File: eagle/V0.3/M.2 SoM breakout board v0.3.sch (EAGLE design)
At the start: 165 parts, among them J1 3-PIN SMD, J10 CON_122_SMD_HEADER, J11 WAFER-HY2.0-4PWB, J12 TP_OPEN, J13 SIM-NANO-4FF, J15 CON_122_SMD_HEADER, J16 SIP-2, J18 PARTICLE-STUDIOS_M_SERIES_M.2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, J19 TP_OPEN, J2 DCJ0202, J20 TP_OPEN, J21 SIP-2, J22 SIP-2, J3 SPARK_CON_30X2_SMD, J5 SCREW-HOLE-3.7, J6 PARTICLE-SZ_PARTICLE-POWER-MO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, J7 SCREW-HOLE-3.7, J8 TP_OPEN, Q3 HSS2333, Q4 HSS2333, Q5 HSS2333, T1 TP_SHORT, U1 XC8107, U2 AT24CS64-SSHM-B, U7 NC, X1 BU-SMA-G, X2 BU-SMA-G, X3 BU-SMA-G

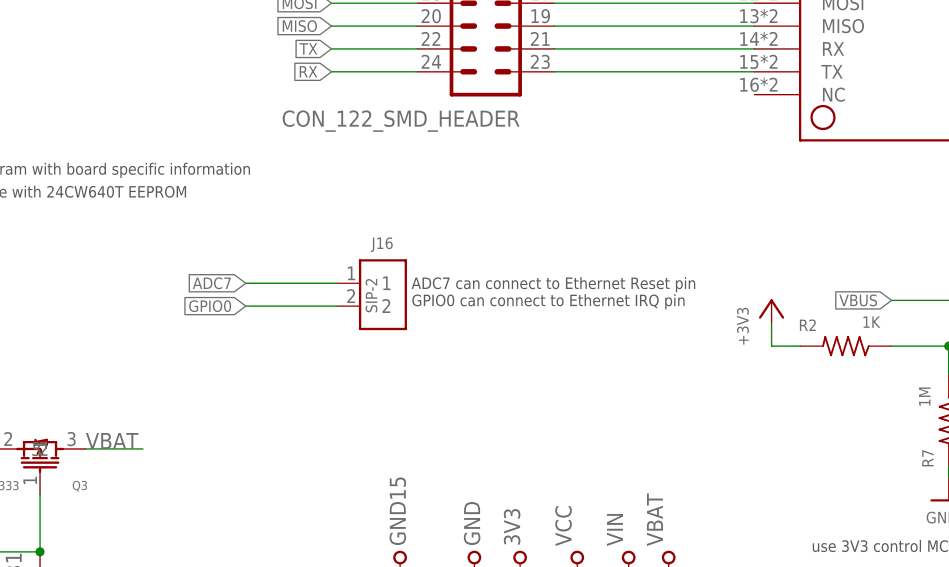
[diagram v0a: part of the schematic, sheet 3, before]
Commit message: update
  delete based test:
  2 pinholes for jumpers ，GPIO0  is used for IRQ ADC7   is used for RESET  that is no needed
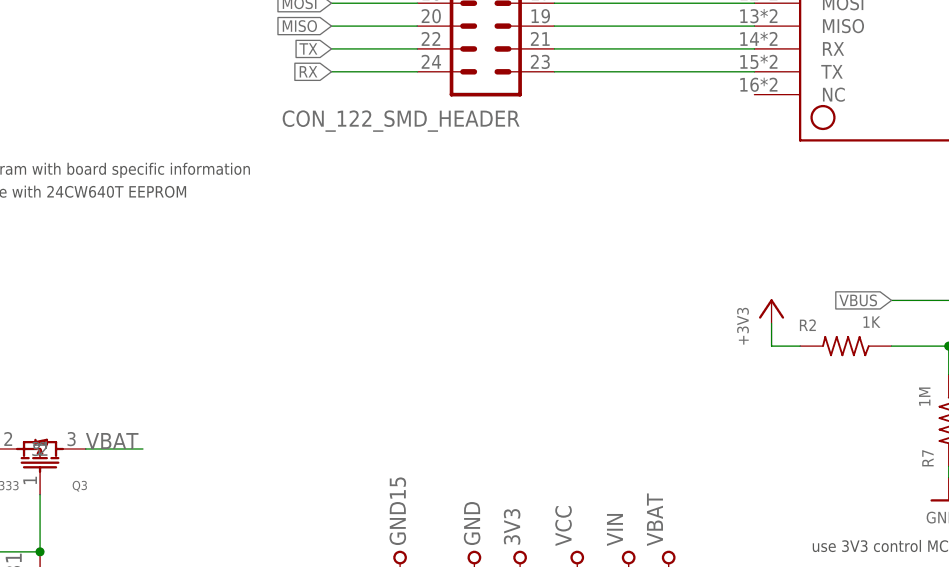
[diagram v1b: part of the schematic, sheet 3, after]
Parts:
- removed J16: SIP-2, particle SZ:SIP-2
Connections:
- net ADC7: no longer J16.1
- net GPIO0: no longer J16.2
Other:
- note removed: "ADC7 can connect to Ethernet Reset pin GPIO0 can connect to Ethernet IRQ pin"
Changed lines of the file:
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@@
 <part name="J1" library="SparkFun-Connectors" library_urn="urn:adsk.eagle:library:513" deviceset="CONN_03" device="JST-SMD" package3d_urn="urn:adsk.eagle:package:38075/1" value="3-PIN SMD"/>
 <part name="JP4" library="particle SZ" library_urn="urn:adsk.eagle:library:21650216" deviceset="TP_SHORT" device="" package3d_urn="urn:adsk.eagle:package:21650878/5"/>
-<part name="J16" library="particle SZ" library_urn="urn:adsk.eagle:library:21650216" deviceset="SIP-2" device="" package3d_urn="urn:adsk.eagle:package:21650858/5"/>
 <part name="JP9" library="particle SZ" library_urn="urn:adsk.eagle:library:21650216" deviceset="TP_SHORT" device="" package3d_urn="urn:adsk.eagle:package:21650878/5" value="TP_SHORT"/>
 </parts>
@@
 </instance>
 <instance part="J18" gate="G$1" x="118.745" y="106.68" smashed="yes">
-<attribute name="NAME" x="98.425" y="53.34" size="1.778" layer="95"/>
-<attribute name="VALUE" x="98.425" y="50.8" size="1.778" layer="96"/>
+<attribute name="NAME" x="99.695" y="53.34" size="1.778" layer="95"/>
+<attribute name="VALUE" x="98.425" y="50.8" size="1.778" layer="96" display="off"/>
 </instance>
 <instance part="J18" gate="G$2" x="53.34" y="102.87" smashed="yes" rot="MR180"/>
@@
 <text x="238.76" y="63.5" size="1.27" layer="97">23 Reserve for reset
 power module</text>
-<text x="125.73" y="104.775" size="1.27" layer="97">ADC7 can connect to Ethernet Reset pin
-GPIO0 can connect to Ethernet IRQ pin</text>
 </plain>
 <instances>
@@
 <attribute name="NAME" x="36.195" y="73.152" size="1.778" layer="95" font="vector" rot="R180"/>
 </instance>
-<instance part="J16" gate="G$1" x="122.555" y="106.045" smashed="yes">
-<attribute name="NAME" x="121.285" y="111.125" size="1.27" layer="95"/>
-<attribute name="VALUE" x="120.65" y="107.95" size="1.27" layer="96" rot="R270"/>
-</instance>
 </instances>
 <busses>
@@
 <pinref part="J10" gate="G$1" pin="19"/>
 </segment>
-<segment>
-<wire x1="117.475" y1="104.775" x2="107.315" y2="104.775" width="0.1524" layer="91"/>
-<label x="107.315" y="104.775" size="1.27" layer="95" rot="R180" xref="yes"/>
-<pinref part="J16" gate="G$1" pin="2"/>
-</segment>
 </net>
 <net name="GPIO1" class="0">
@@
 </segment>
 </net>
-<net name="ADC7" class="0">
-<segment>
-<wire x1="117.475" y1="107.315" x2="107.315" y2="107.315" width="0.1524" layer="91"/>
-<label x="107.315" y="107.315" size="1.27" layer="95" rot="R180" xref="yes"/>
-<pinref part="J16" gate="G$1" pin="1"/>
-</segment>
-</net>

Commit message: update
update SCH&PCB
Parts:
- removed J8: TP_OPEN, particle SZ:TP_OPEN
- removed JP9: TP_SHORT, particle SZ:TP_SHORT
- removed LED2: BLUE, particle SZ:LED
- removed R22: 10K, particle-studios:RES_10K_0603
- removed R32: nc, particle SZ:RES0402S
- added Q1: HSS2333, RedBear:PMOS
- added R17: 1K, Particle:R-US_
- added TP1, TP2, TP5, TP8: TPTPEB, particle SZ:TPTPEB
- R11: value 1K -> 100K
- R18: value nc -> 6.91K; device particle SZ:RES0402S -> particle SZ:RESR0603
- R74: value nc -> 83.2K; device particle SZ:RES0402S -> particle SZ:RESR0603
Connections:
- removed net 5VDC: J6.5DC@3, J6.5DC@4
- removed net N$44: R16.2, T1.2
- removed net N$59: JP9.2, R11.2
- removed net NC: J6.NC@8
- new net 3V3_AUX: J11.2, J3.8, J4.2, J6.3V3@2, MS1.3V3, TP30.PP
- net +3V3: no longer J11.2, J3.8, J4.2, J6.3V3@2, MS1.3V3, TP30.PP
- net GND: now also TP8.1; no longer LED2.K, R22.1
- net GPIO1: now also J6.REGN@7
- net N$13: now also J21.2, TP2.1, TP5.1; no longer R32.1
- net N$14: now also Q1.2, R11.2, T1.2; no longer J8.2, R32.2
- net N$18: now also Q1.3, R16.2; no longer R15.1, S1.3, S1.6
- net N$36: now also Q1.1, R17.2; no longer LED2.A
- net N$57: now also R15.1, R17.1, S1.3, S1.6; no longer J21.2, R22.2
- net PWM3: no longer JP9.1
- net REGN: now also J6.NC@8, TP1.1; no longer J6.REGN@7
- net TS: no longer J8.1
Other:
- note added: "GPIO1 is used for ctroling the power module EN_AUX which make load switch work"
- note removed: "If LiPo TS pin don't have 10K NTC connect to GND, connect this jumper,"
- moved on the sheet: 3V3, D17, D4, F5, GND, GND15, J1, J2, J21, J5, J7, Q3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

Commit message: update
update PCB&SCH
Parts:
- added R22: NC, Particle:R-US_
- added RT1: 6.91K, particle SZ:RESR0603
- J11: device M.2 SoM breakout board v0.2-0228:WAFER-HY2.0-4PWB -> M.2 SoM breakout board v0.3:M.2-SOM-BREAKOUT-BOARD-V0.2-0228_WAFER-HY2.0-4PWB
- R18: value 6.91K -> NC; device particle SZ:RESR0603 -> Particle:R-US_
- renumbered R74 to RT2
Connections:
- removed net N$19 (its old number): LED1.A, R16.1
- new net N$36: LED1.K, Q1.2, R22.2
- new net N$44: J6.5DC@3
- new net N$59: J6.5DC@4
- net GND: now also Q1.3, R17.1, R22.1; no longer LED1.K
- net N$13: now also RT1.1; no longer R18.1
- net N$14: now also R16.2; no longer Q1.2, R11.2
- net N$18: now also LED1.A, R16.1, R18.1; no longer Q1.3, R16.2
- net N$57: no longer R17.1
- net PWM1: now also J10.7; no longer J10.11
- net PWM2: now also J10.11; no longer J10.7
- net REGN: now also RT1.2; no longer R18.2
- net VIN: now also R11.2, R18.2
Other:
- note added: "0.3 version"
- note added: "1.3V3 is divided into one channel as the load conversion switch 3V3_AUX, and GPIO1 is added to control EN_AUX 2. Change the peripheral power supply to load 3V3_AUX 3. Remove LED2 (required by nick) 4.LED1 only lights up when DC_JACK, add NMOS control 5. Modify the TS pin configuration and add reserved plug-in resistor vacancies. 6.J10 exchanges the positions of PWM1 and PWM2 and aligns with pinma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"
- note removed: "10"
- note removed: "11"
- note removed: "4"
- note removed: "5"
- note removed: "6"
- note removed: "7"
- note removed: "8"
- note removed: "9"
- moved on the sheet: J11, LED1, Q1, R11, R16, R17, T1

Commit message: Update
Update SCH&PCB
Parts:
- F5: device adafruit:PTCFUSE-1206 -> adafruit:PTCFUSE-1812
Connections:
- net !RESET: now also J15.2
- net SOM17: no longer J15.2
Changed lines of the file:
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@@
 <layer number="13" name="Route13" color="21" fill="1" visible="no" active="no"/>
 <layer number="14" name="Route14" color="22" fill="1" visible="no" active="no"/>
-<layer number="15" name="Route15" color="23" fill="1" visible="no" active="no"/>
+<layer number="15" name="Route15" color="30" fill="1" visible="no" active="no"/>
 <layer number="16" name="Bottom" color="1" fill="1" visible="no" active="no"/>
 <layer number="17" name="Pads" color="2" fill="1" visible="no" active="no"/>
@@
 <part name="D17" library="particle-studios" library_urn="urn:adsk.eagle:library:10700396" deviceset="DIODE-ZENER" device="" package3d_urn="urn:adsk.eagle:package:18150248/1" value="SMAJ15CA-13-F"/>
 <part name="GND3" library="supply1" deviceset="GND" device=""/>
-<part name="F5" library="adafruit" library_urn="urn:adsk.eagle:library:420" deviceset="PTCFUSE" device="-1206" package3d_urn="urn:adsk.eagle:package:6240569/1" value="16V/0.75A"/>
+<part name="F5" library="adafruit" library_urn="urn:adsk.eagle:library:420" deviceset="PTCFUSE" device="-1812" package3d_urn="urn:adsk.eagle:package:6240348/1" value="16V/0.75A"/>
 <part name="U$5" library="microbuilder" deviceset="GND" device=""/>
 <part name="U$8" library="microbuilder" deviceset="GND" device=""/>
@@
 6.J10 exchanges the positions of
  PWM1 and PWM2 and aligns with pinmap
-7. modify the layout</text>
+7. modify the layout
+8.change the reset PIN of featherWing</text>
 </plain>
 <instances>
@@
 <pinref part="J6" gate="G$1" pin="!RST@23"/>
 </segment>
+<segment>
+<wire x1="126.365" y1="158.75" x2="116.84" y2="158.75" width="0.1524" layer="91"/>
+<label x="116.84" y="158.75" size="1.27" layer="95" rot="R180" xref="yes"/>
+<pinref part="J15" gate="G$1" pin="2"/>
+</segment>
 </net>
 <net name="N$45" class="0">
@@
 </segment>
 </net>
-<net name="SOM17" class="0">
-<segment>
-<wire x1="126.365" y1="158.75" x2="116.84" y2="158.75" width="0.1524" layer="91"/>
-<label x="116.84" y="158.75" size="1.27" layer="95" rot="R180" xref="yes"/>
-<pinref part="J15" gate="G$1" pin="2"/>
-</segment>
-</net>

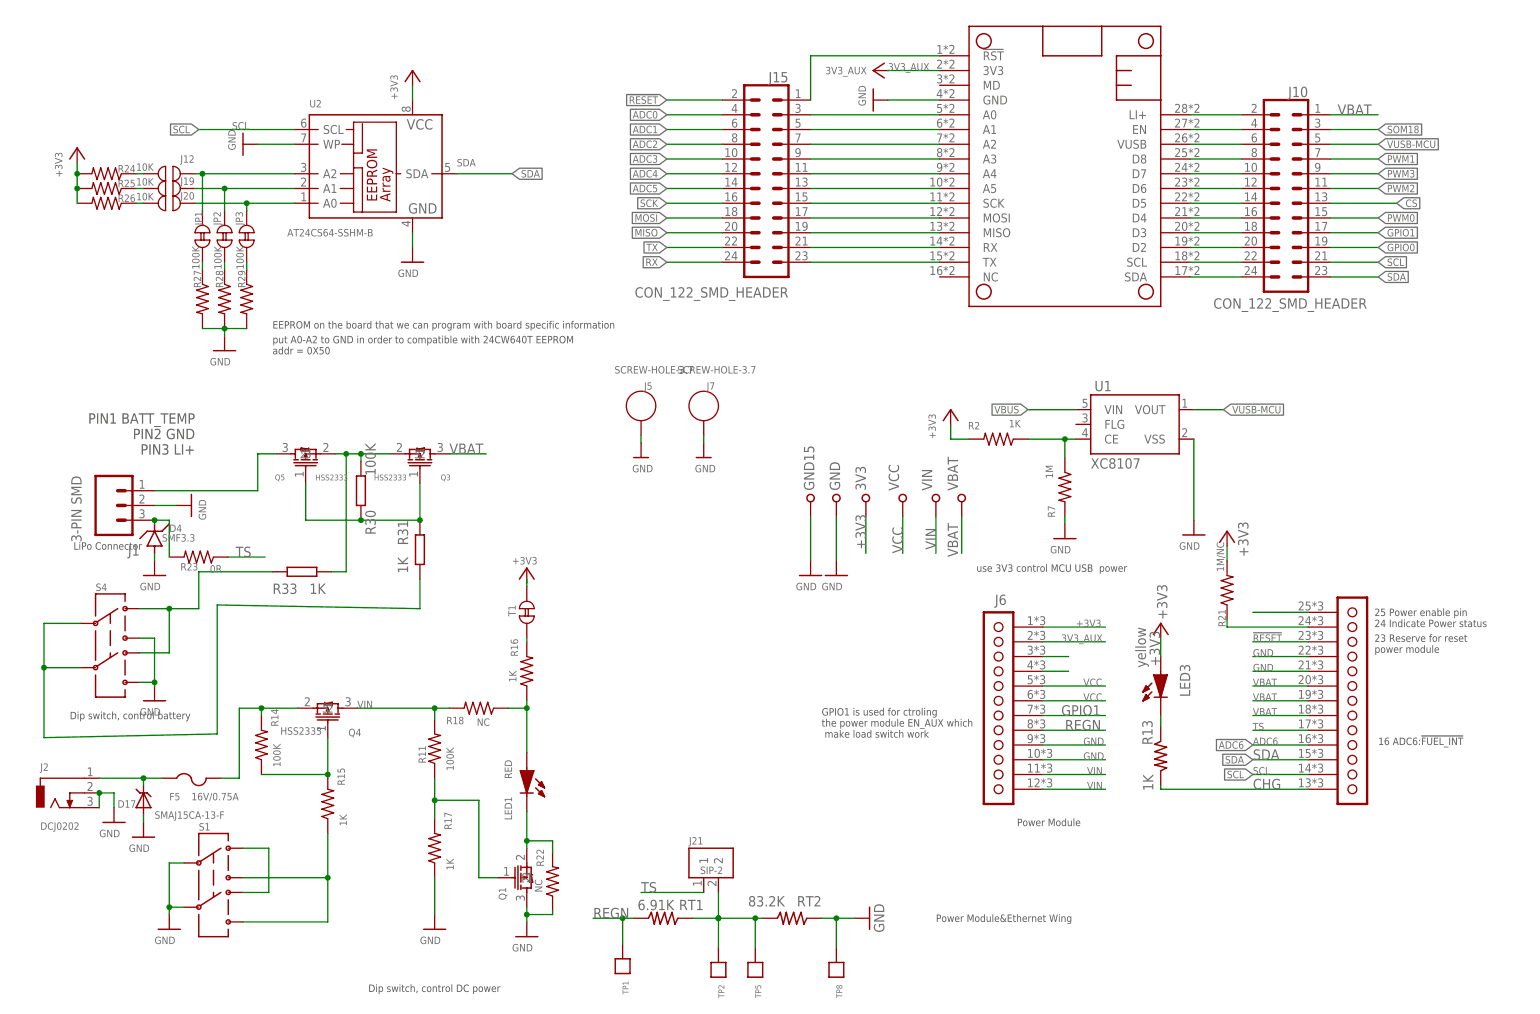
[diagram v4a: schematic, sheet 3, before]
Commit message: updated v0.3 design
1. Change feather jumpers to smd scratch pads
2. Align proto area with m.2
3. Add 3.3V and GND rail along the proto area
4. LiPo battery pinout change - when we changed from vertical to horizontal, the pinout was flipped. so this is now fixed.
5. Flipped the TX/RX to match the feather pin out
6. Removed EN pin connection to feather
7. Align RGB LED and buttons
8. Align the mounting holes to the corners of the PCB
9. Updated silkscreen and pinout labels on top and bottom
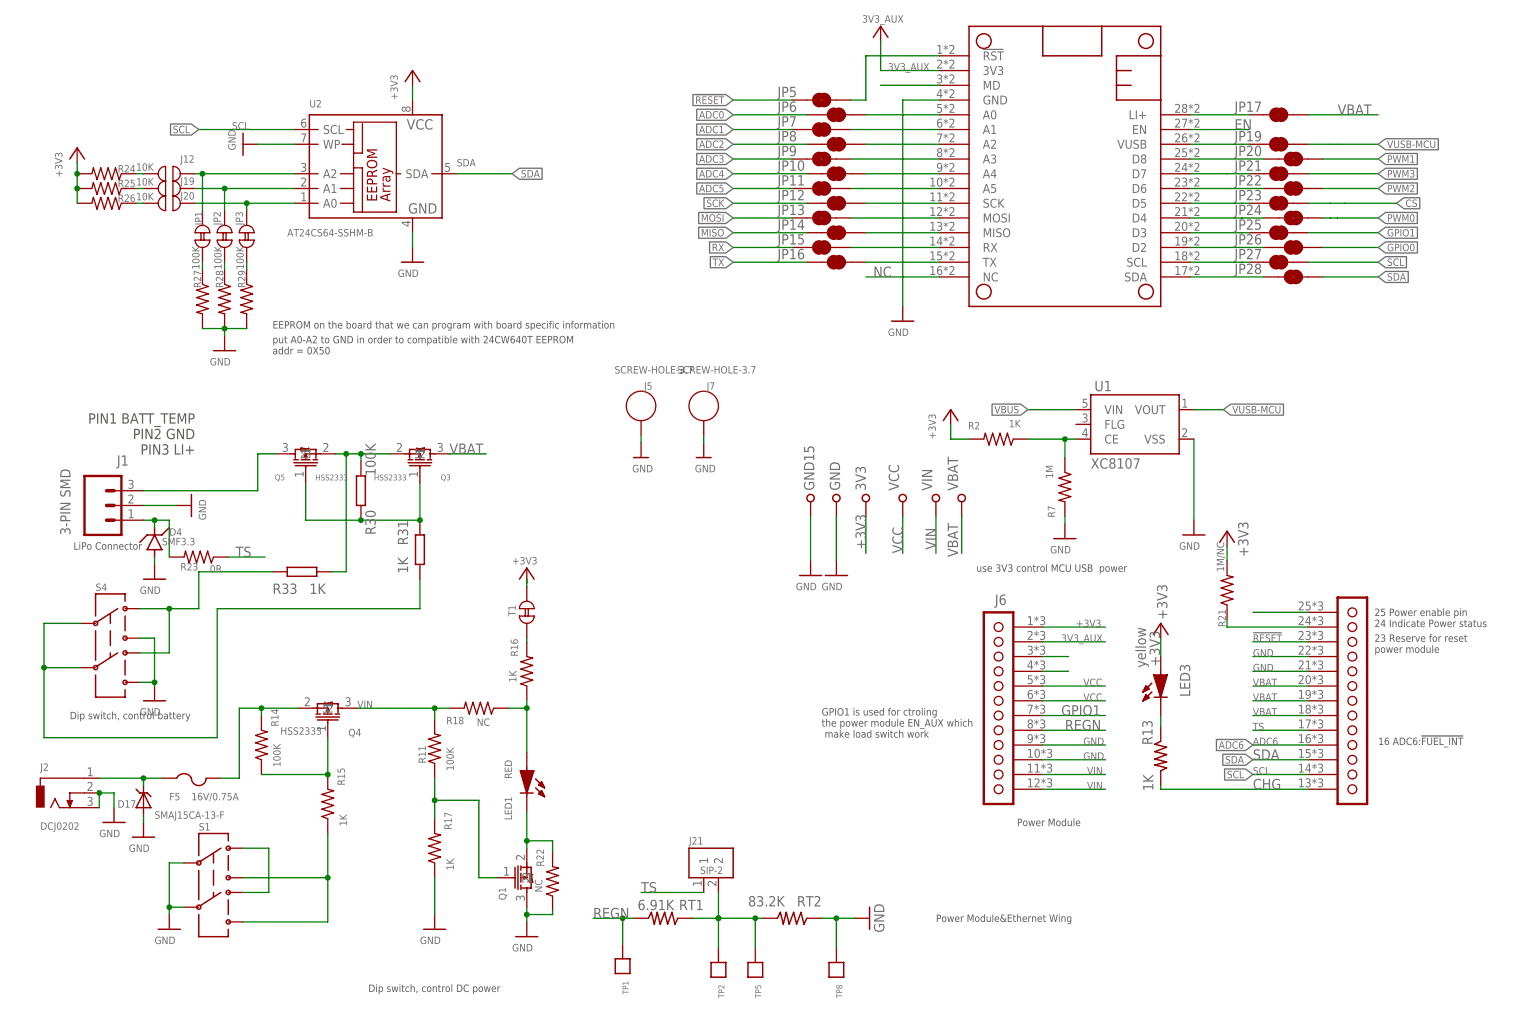
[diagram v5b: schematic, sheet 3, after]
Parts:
- removed J10, J15: CON_122_SMD_HEADER, Spark:CON_122_SMD_HEADER
- added JP10, JP11, JP12, JP13, JP14, JP15, JP16, JP17, JP19, JP20, JP21, JP22, JP23, JP24, JP25, JP26, JP27, JP28, JP5, JP6, JP7, JP8, JP9: JUMPER-SMT_2_NC_TRACE_NO-SILK, SparkFun-Jumpers:JUMPER-SMT_2_NC_TRACE_NO-SILK
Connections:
- removed net N$43: J10.4, MS1.EN
- new net EN: MS1.EN
- new net N$223: D4.C, J1.1, R23.2
- new net NC: MS1.NC
- net !RESET: now also JP5.1; no longer J15.2
- net ADC0: now also JP6.1; no longer J15.4
- net ADC1: now also JP7.1; no longer J15.6
- net ADC2: now also JP8.1; no longer J15.8
- net ADC3: now also JP9.1; no longer J15.10
- net ADC4: now also JP10.1; no longer J15.12
- net ADC5: now also JP11.1; no longer J15.14
- net CS: now also JP23.2; no longer J10.13
- net GPIO0: now also JP26.2; no longer J10.19
- net GPIO1: now also JP25.2; no longer J10.17
- net LI+: now also JP17.1; no longer J10.2
- net MISO: now also JP14.1; no longer J15.20
- net MOSI: now also JP13.1; no longer J15.18
- net N$16: now also JP21.1; no longer J10.10
- net N$21: now also JP6.2; no longer J15.3
- net N$23: now also JP7.2; no longer J15.5
- net N$24: now also JP8.2; no longer J15.7
- net N$25: now also JP9.2; no longer J15.9
- net N$26: now also JP10.2; no longer J15.11
- net N$27: now also JP11.2; no longer J15.13
- net N$28: now also JP12.2; no longer J15.15
- net N$29: now also JP13.2; no longer J15.17
- net N$30: now also JP14.2; no longer J15.19
- net N$31: now also JP15.2; no longer J15.21
- net N$32: now also JP16.2; no longer J15.23
- net N$34: now also JP28.1; no longer J10.24
- net N$35: now also JP27.1; no longer J10.22
- net N$37: now also JP26.1; no longer J10.20
- net N$38: now also JP25.1; no longer J10.18
- net N$39: now also JP24.1; no longer J10.16
- net N$40: now also JP23.1; no longer J10.14
- net N$41: now also JP22.1; no longer J10.12
- net N$42: now also JP20.1; no longer J10.8
- net N$46: now also JP5.2; no longer J15.1
- net N$58: now also J1.3; no longer J1.1
- net N$7: now also MS1.MD; no longer D4.C, J1.3, R23.2
- net PWM0: now also JP24.2; no longer J10.15
- net PWM1: now also JP20.2; no longer J10.7
- net PWM2: now also JP22.2; no longer J10.11
- net PWM3: now also JP21.2; no longer J10.9
- net RX: now also JP15.1; no longer J15.24
- net SCK: now also JP12.1; no longer J15.16
- net SCL: now also JP27.2; no longer J10.21
- net SDA: now also JP28.2; no longer J10.23
- net SOM18: no longer J10.3
- net TX: now also JP16.1; no longer J15.22
- net V-USB: now also JP19.1; no longer J10.6
- net VBAT: now also JP17.2; no longer J10.1
- net VUSB-MCU: now also JP19.2; no longer J10.5
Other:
- moved on the sheet: D4, J1

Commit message: update
update
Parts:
- removed TP10, TP11, TP12, TP13, TP14, TP15, TP16, TP17, TP18, TP19, TP20, TP21, TP22, TP23, TP24, TP25, TP26, TP27, TP28, TP29, TP3, TP30, TP31, TP32, TP33, TP34, TP35, TP36, TP37, TP38, TP39, TP4, TP40, TP41, TP42, TP43, TP44, TP45, TP46, TP47, TP48, TP49, TP50, TP51, TP52, TP53, TP54, TP57, TP6, TP7, TP9: TPSB1,27, testpad:TPSB1,27
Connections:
- net !MODE: no longer TP35.PP
- net !RESET: no longer TP36.PP
- net 3V3_AUX: no longer TP30.PP
- net ADC0: no longer TP6.PP
- net ADC1: no longer TP7.PP
- net ADC2: no longer TP9.PP
- net ADC3: no longer TP10.PP
- net ADC4: no longer TP12.PP
- net ADC5: no longer TP13.PP
- net ADC7: no longer TP15.PP
- net CS: no longer TP41.PP
- net CTS: no longer TP39.PP
- net GND: no longer TP11.PP, TP16.PP, TP29.PP, TP45.PP
- net GPIO0: no longer TP48.PP
- net GPIO1: no longer TP49.PP
- net LED_BLUE: no longer TP24.PP
- net LED_GREEN: no longer TP23.PP
- net LED_RED: no longer TP22.PP
- net MISO: no longer TP42.PP
- net MOSI: no longer TP43.PP
- net N$15: no longer TP14.PP
- net NFC1: no longer TP3.PP
- net NFC2: no longer TP4.PP
- net PWM0: no longer TP50.PP
- net PWM1: no longer TP51.PP
- net PWM2: no longer TP52.PP
- net PWM3: no longer TP53.PP
- net RTS: no longer TP40.PP
- net RX: no longer TP38.PP
- net SCK: no longer TP44.PP
- net SCL: no longer TP33.PP
- net SDA: no longer TP34.PP
- net SOM10: no longer TP31.PP
- net SOM11: no longer TP32.PP
- net SOM12: no longer TP46.PP
- net SOM13: no longer TP47.PP
- net SOM14: no longer TP17.PP
- net SOM15: no longer TP18.PP
- net SOM16: no longer TP19.PP
- net SOM17: no longer TP20.PP
- net SOM18: no longer TP21.PP
- net SOM5: no longer TP25.PP
- net SOM6: no longer TP26.PP
- net SOM7: no longer TP27.PP
- net SOM8: no longer TP28.PP
- net SOM9: no longer TP57.PP
- net TX: no longer TP37.PP
- net VCC: no longer TP54.PP
